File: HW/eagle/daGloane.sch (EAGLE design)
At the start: 64 parts, among them IC1 MCP1252-33X50, U1 STM32F10XTXU6, X2 SPARKFUN-CONNECTORS_USB-MICROB

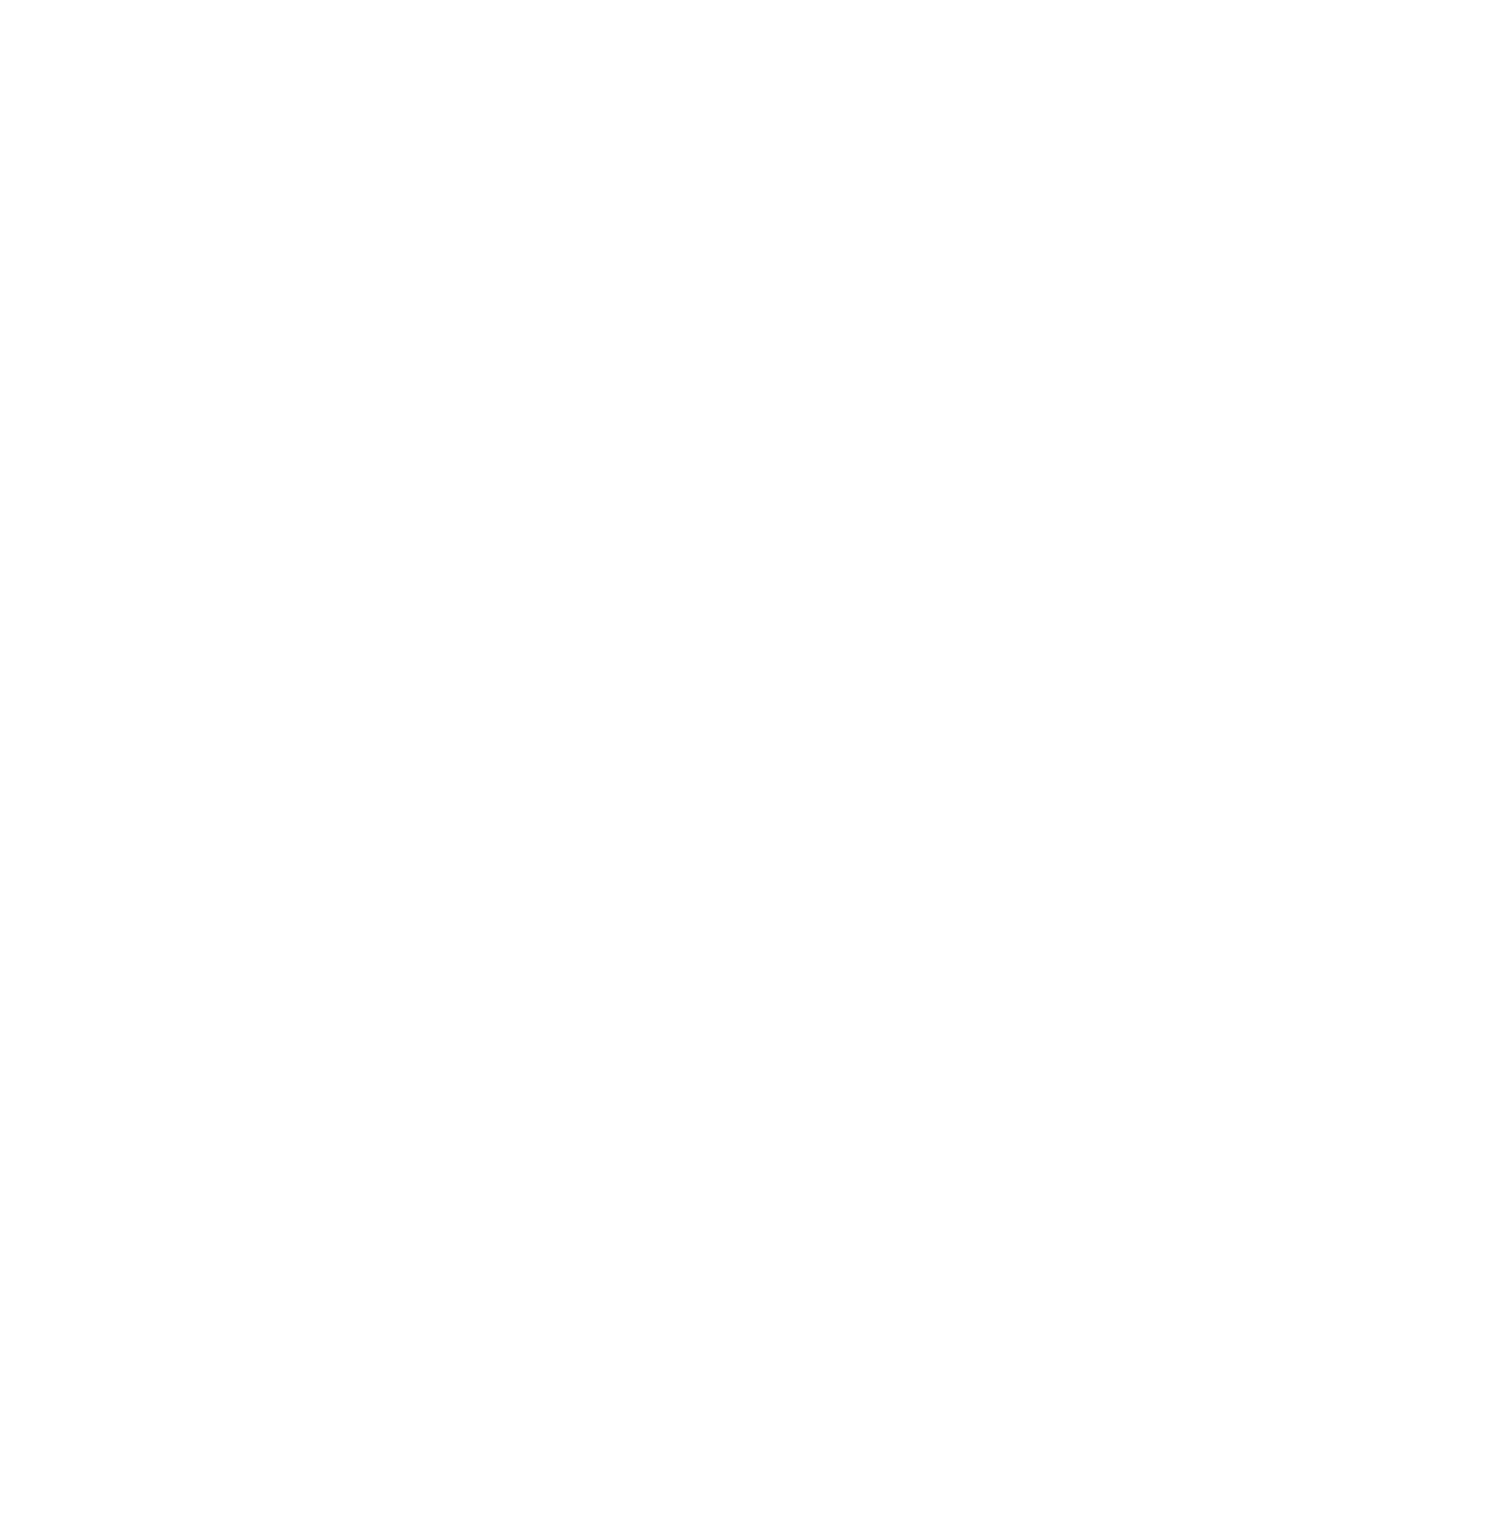
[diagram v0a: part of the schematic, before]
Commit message: frame with bldc drive version added to schematic
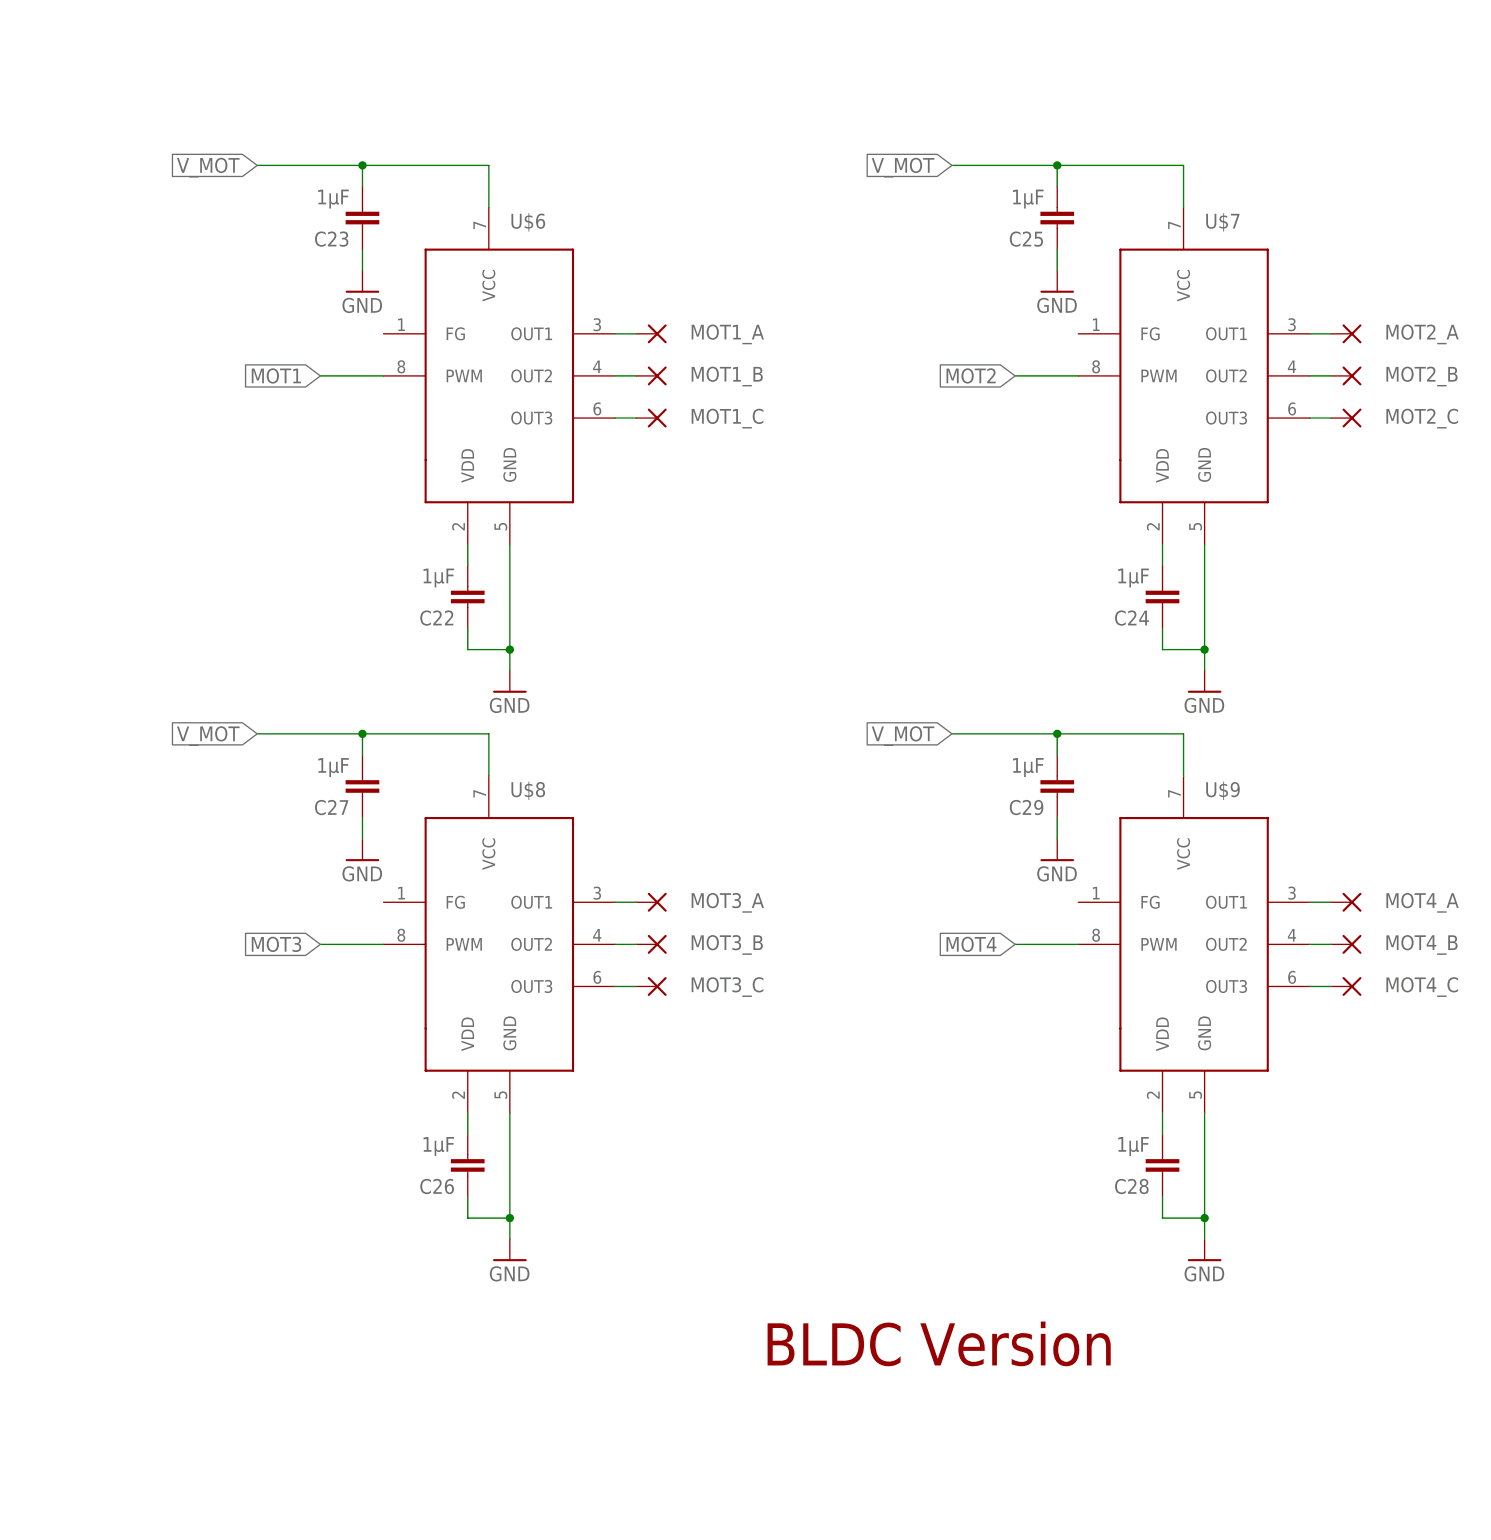
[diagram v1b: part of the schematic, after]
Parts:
- added C22, C23, C24, C25, C26, C27, C28, C29: 1µF, rcl:C-EUC0603
- added MOT1_A, MOT1_B, MOT1_C, MOT2_A, MOT2_B, MOT2_C, MOT3_A, MOT3_B, MOT3_C, MOT4_A, MOT4_B, MOT4_C: WIREPAD1,6/0,8, wirepad:WIREPAD1,6/0,8
- added U$6, U$7, U$8, U$9: MTD6501C, daGloane:MTD6501C
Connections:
- new net MOT1_A: MOT1_A.P, U$6.OUT1
- new net MOT1_A1: MOT2_A.P, U$7.OUT1
- new net MOT1_A2: MOT3_A.P, U$8.OUT1
- new net MOT1_A3: MOT4_A.P, U$9.OUT1
- new net N$26: C22.2, U$6.VDD
- new net N$27: MOT1_B.P, U$6.OUT2
- new net N$29: MOT1_C.P, U$6.OUT3
- new net N$30: MOT2_B.P, U$7.OUT2
- new net N$31: MOT2_C.P, U$7.OUT3
- new net N$32: C24.2, U$7.VDD
- new net N$33: MOT3_B.P, U$8.OUT2
- new net N$34: MOT3_C.P, U$8.OUT3
- new net N$35: C26.2, U$8.VDD
- new net N$36: MOT4_B.P, U$9.OUT2
- new net N$37: MOT4_C.P, U$9.OUT3
- new net N$38: C28.2, U$9.VDD
- new net V_MOT: C23.2, C25.2, C27.2, C29.2, U$6.VCC, U$7.VCC, U$8.VCC, U$9.VCC
- net GND: now also C22.1, C23.1, C24.1, C25.1, C26.1, C27.1, C28.1, C29.1, U$6.GND, U$7.GND, U$8.GND, U$9.GND
- net MOT1: now also U$6.PWM
- net MOT2: now also U$7.PWM
- net MOT3: now also U$8.PWM
- net MOT4: now also U$9.PWM
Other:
- note added: "BLDC Version"

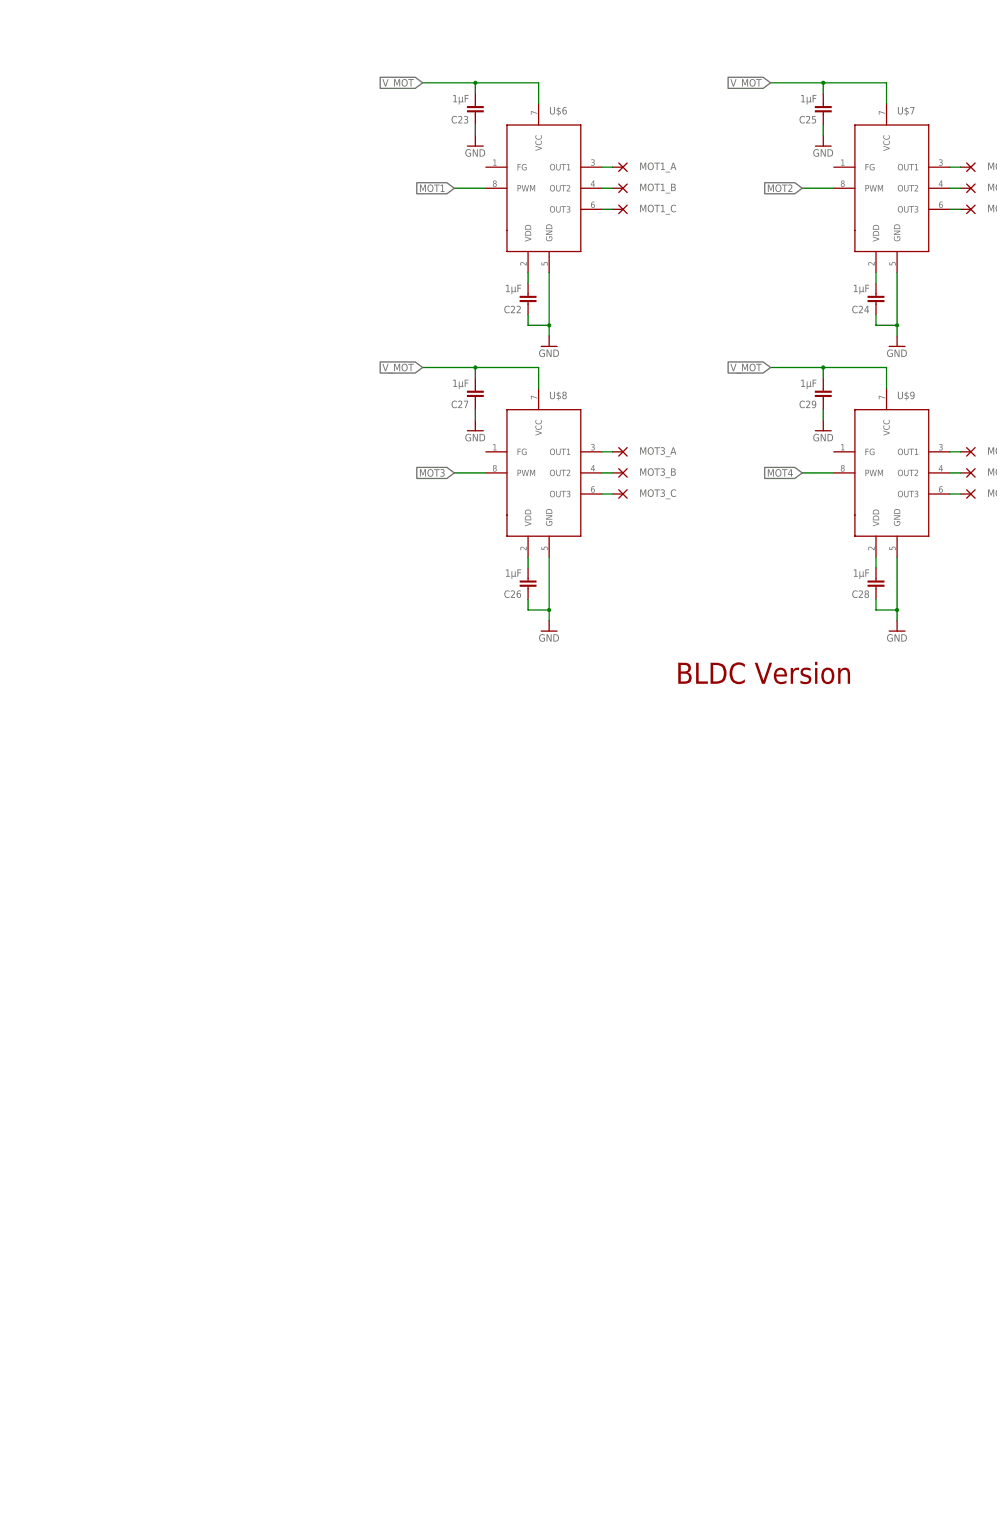
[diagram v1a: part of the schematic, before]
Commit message: DC motor drive added to schematic
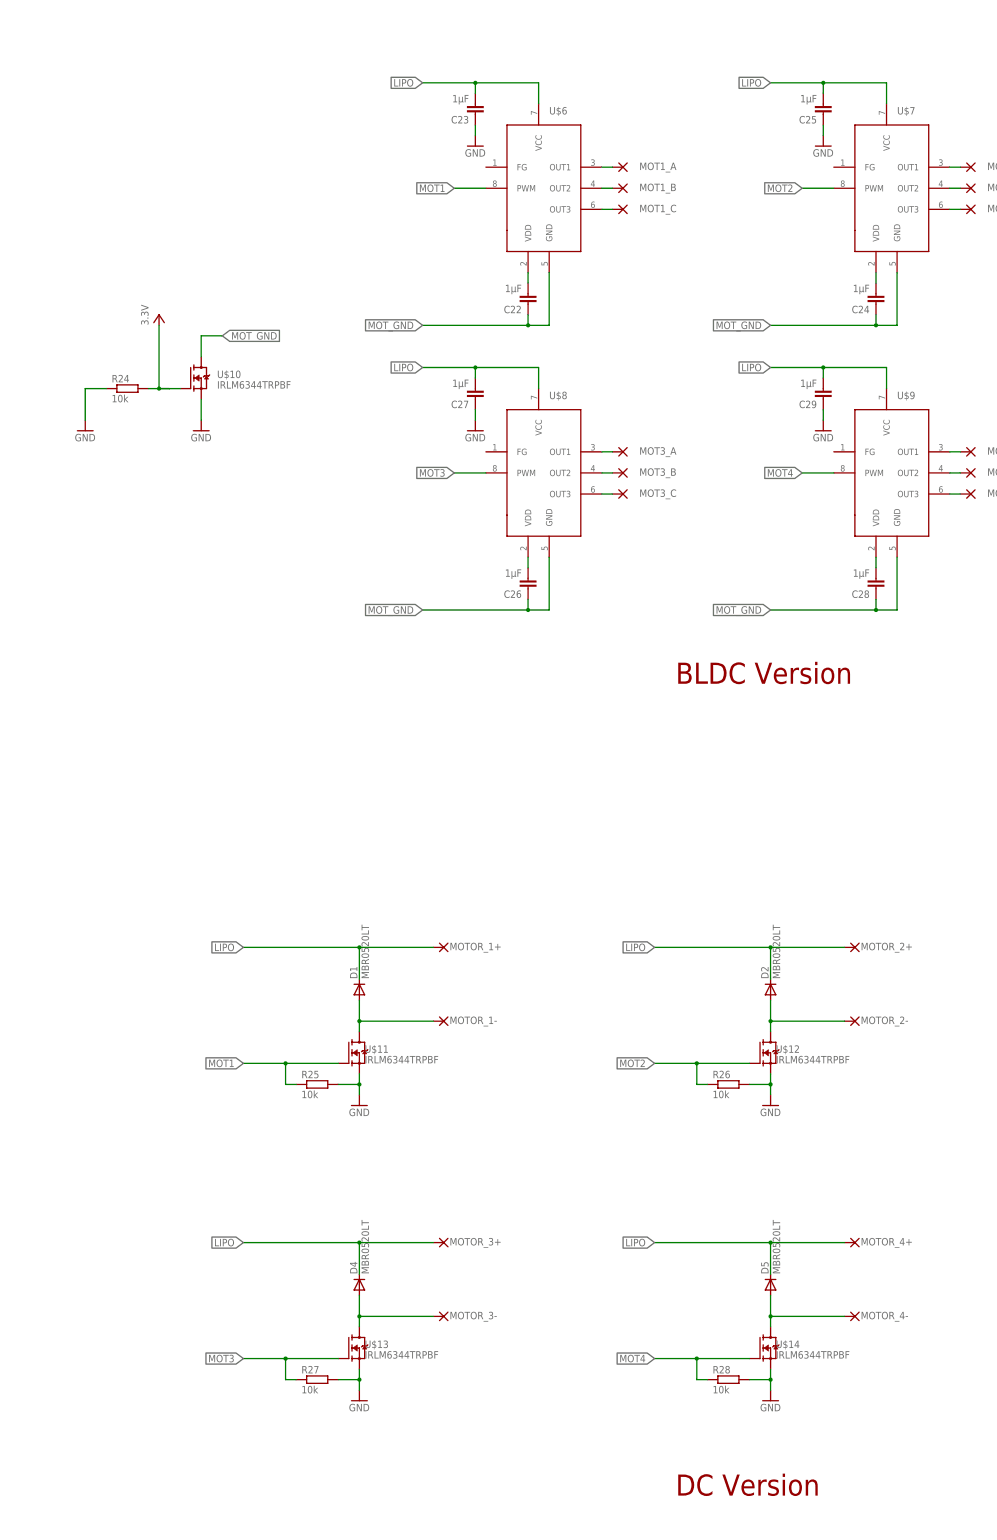
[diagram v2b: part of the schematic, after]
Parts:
- added D1, D2, D4, D5: MBR0520LT, diode:MBR0520LT
- added MOTOR_1+, MOTOR_1-, MOTOR_2+, MOTOR_2-, MOTOR_3+, MOTOR_3-, MOTOR_4+, MOTOR_4-: WIREPAD1,6/0,8, wirepad:WIREPAD1,6/0,8
- added R24, R25, R26, R27, R28: 10k, rcl:R-EU_R0603
- added U$10, U$11, U$12, U$13, U$14: IRLM6344TRPBF, daGloane:IRLM6344TRPBF
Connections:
- removed net V_MOT: C23.2, C25.2, C27.2, C29.2, U$6.VCC, U$7.VCC, U$8.VCC, U$9.VCC
- new net MOT_GND: C22.1, C24.1, C26.1, C28.1, U$10.D, U$6.GND, U$7.GND, U$8.GND, U$9.GND
- new net N$39: D1.A, MOTOR_1-.P, U$11.D
- new net N$40: D2.A, MOTOR_2-.P, U$12.D
- new net N$41: D4.A, MOTOR_3-.P, U$13.D
- new net N$42: D5.A, MOTOR_4-.P, U$14.D
- net GND: now also R24.1, R25.2, R26.2, R27.2, R28.2, U$10.S, U$11.S, U$12.S, U$13.S, U$14.S; no longer C22.1, C24.1, C26.1, C28.1, U$6.GND, U$7.GND, U$8.GND, U$9.GND
- net LIPO: now also C23.2, C25.2, C27.2, C29.2, D1.C, D2.C, D4.C, D5.C, MOTOR_1+.P, MOTOR_2+.P, MOTOR_3+.P, MOTOR_4+.P, U$6.VCC, U$7.VCC, U$8.VCC, U$9.VCC
- net MOT1: now also R25.1, U$11.G
- net MOT2: now also R26.1, U$12.G
- net MOT3: now also R27.1, U$13.G
- net MOT4: now also R28.1, U$14.G
- net VCC: now also R24.2, U$10.G
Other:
- note added: "DC Version"
